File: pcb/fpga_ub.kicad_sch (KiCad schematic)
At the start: 9 parts, among them J1201 Conn_02x07_Top_Bottom, U666 XC7A75T-FTG256

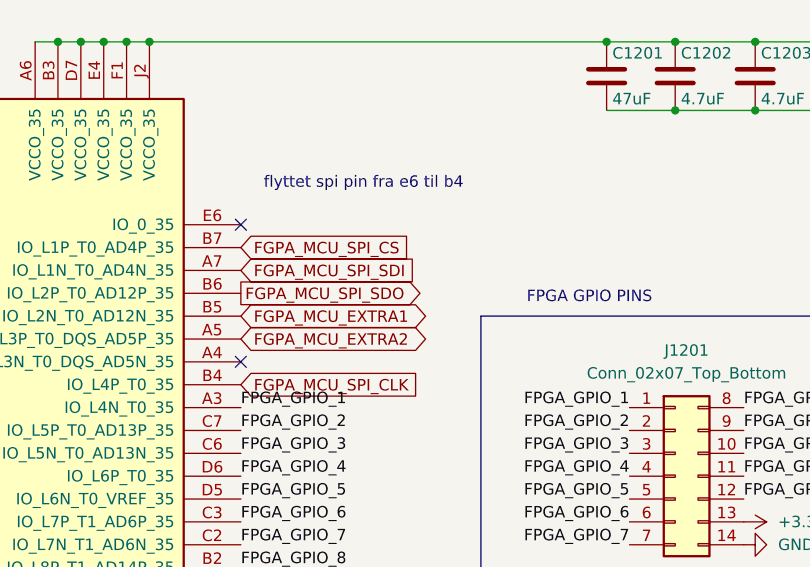
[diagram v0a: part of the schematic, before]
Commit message: fix vga resistors
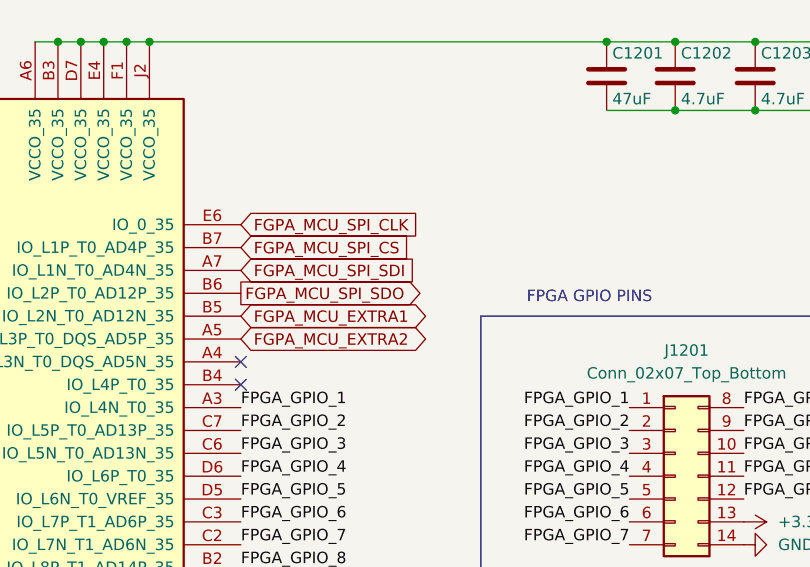
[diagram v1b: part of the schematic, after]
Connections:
- net FGPA_MCU_SPI_CLK: now also U666.E6 (IO_0_35); no longer U666.B4 (IO_L4P_T0_35)
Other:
- note removed: "flyttet spi pin fra e6 til b4"
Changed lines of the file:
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@@
   (no_connect (at 43.18 67.31))
   (no_connect (at 144.78 92.71))
-  (no_connect (at 144.78 41.91))
   (no_connect (at 144.78 57.15))
+  (no_connect (at 144.78 59.69))
   (no_connect (at 43.18 41.91))
   (no_connect (at 43.18 44.45))
@@
     (effects (font (size 1.27 1.27)) (justify left bottom))
   )
-  (text "flyttet spi pin fra e6 til b4\n" (at 147.32 38.1 0)
-    (effects (font (size 1.27 1.27)) (justify left bottom))
-  )
   (label "FPGA_GPIO_2" (at 144.78 64.77 0)
     (effects (font (size 1.27 1.27)) (justify left bottom))
@@
     )
   )
-  (global_label "FGPA_MCU_SPI_CLK" (shape input) (at 144.78 59.69 0) (fields_autoplaced)
-    (effects (font (size 1.27 1.27)) (justify left))
-    (property "Intersheet References" "${INTERSHEET_REFS}" (id 0) (at 165.5174 59.6106 0)
-      (effects (font (size 1.27 1.27)) (justify left) hide)
-    )
-  )
   (global_label "FPGA_DEBUG_LED_BLOCK35_1" (shape input) (at 151.13 130.81 0) (fields_autoplaced)
     (effects (font (size 1.27 1.27)) (justify left))
@@
       (effects (font (size 1.27 1.27)) (justify left) hide)
     )
+  )
+  (global_label "FGPA_MCU_SPI_CLK" (shape input) (at 144.78 41.91 0) (fields_autoplaced)
+    (effects (font (size 1.27 1.27)) (justify left))
+    (property "Intersheet References" "${INTERSHEET_REFS}" (id 0) (at 165.5174 41.8306 0)
+      (effects (font (size 1.27 1.27)) (justify left) hide)
+    )
